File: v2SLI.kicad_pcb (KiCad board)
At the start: 2 copper layers, 77.7 x 75.9 mm, 61 parts, among them J1 Inter-MCU Interrupts Header, J10 Programming Header for 205, J11 Boot 0, J12 Boot 1, J13 Boot 1, J14 Programming Header for 103, J15 Boot 0, J16 SPI Bus, J17 Enable Fix, J18 GPIOs, J19 UART1, J2 Inter-MCU UART Header, J20 Micro_SD_Card, J21 Radio UART, J22 VCC RAIL, J23 GND RAIL, J3 SPI Bus, J4 UART1, J5 205GPIOs, J6 UART2, J7 I2C1, J8 Conn_02x15_Top_Bottom, J9 Conn_02x15_Top_Bottom, SW1 SW_Push, SW2 SW_Push, SW3 SW_Push, U1 STM32F205RETx, U2 BMP388, U3 BMP388, U4 ICM20948, U5 TCR2EE185-SOT553, U6 ADA746, U7 STM32F103C8Tx, U8 Xbee

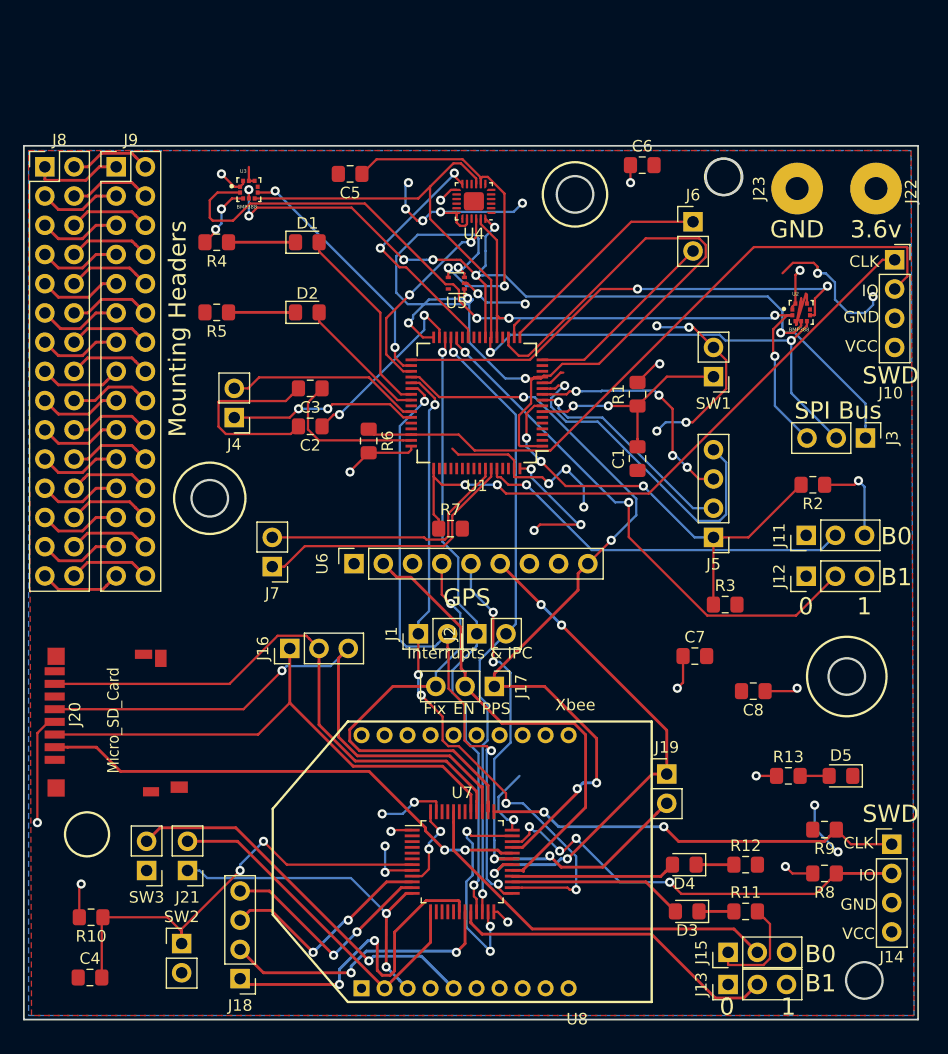
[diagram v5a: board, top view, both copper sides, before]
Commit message: Added some logos for our sponsors and some holes for mouting
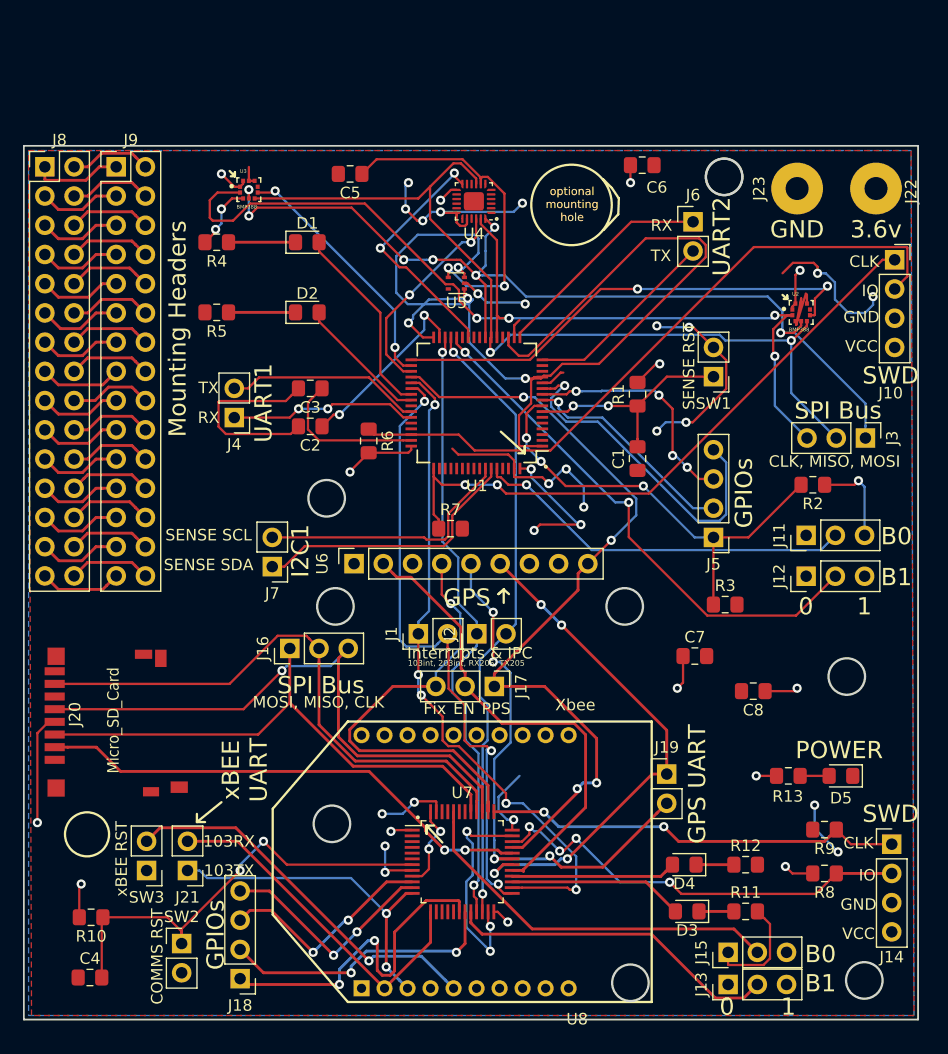
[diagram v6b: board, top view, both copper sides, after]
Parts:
- removed the G*** at (164.2, 90.6)
- added G***: LOGO, images:cougar, B.Cu at (186.5, 85.3)
- added G***: LOGO, images:iridium1000dpi, B.Cu at (162.3, 47.3)
- added G***: LOGO, images:Untitled, B.Cu at (155.9, 70.2)
- added G***: LOGO, images:kamannegative, B.Cu at (187.8, 60.6)
- added G***: LOGO, images:rlbetter, B.Cu at (163.0, 95.2)
- added REF**: OSHW-Symbol_6.7x6mm_SilkScreen, Symbol:OSHW-Symbol_6.7x6mm_SilkScreen, B.Cu at (128.1, 84.6)
- added REF**: ESD-Logo_6.6x6mm_SilkScreen, Symbol:ESD-Logo_6.6x6mm_SilkScreen, B.Cu at (128.6, 77.3)
- added REF**: WEEE-Logo_4.2x6mm_SilkScreen, Symbol:WEEE-Logo_4.2x6mm_SilkScreen, B.Cu at (132.0, 106.1)
- added REF**: KiCad-Logo2_6mm_SilkScreen, Symbol:KiCad-Logo2_6mm_SilkScreen, B.Cu at (132.0, 96.2)
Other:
- outline, holes or cut-outs redrawn
- board text added: "103RX"
- board text added: "103TX"
- board text added: "103int, 203int, RX205, TX205"
- board text added: "CLK, MISO, MOSI"
- board text added: "COMMS RST"
- board text added: "GPIOs"
- board text added: "GPS UART"
- board text added: "I2C1"
- board text added: "MOSI, MISO, CLK"
- board text added: "POWER"
- board text added: "RX"
- board text added: "SENSE RST"
- board text added: "SENSE SCL"
- board text added: "SENSE SDA"
- board text added: "Sponsored By:"
- board text added: "TX"
- board text added: "UART1"
- board text added: "UART2"
- board text added: "optional mounting hole"
- board text added: "xBEE RST"
- board text added: "xBEE UART"
